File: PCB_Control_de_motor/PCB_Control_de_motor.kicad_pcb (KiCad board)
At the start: 2 copper layers, 71 x 45.5 mm, 50 parts, among them IC1 ESP32-S3-WROOM-1-N16, IC2 USBLC6-2SC6, IC3 DRV8871DDAR, IC4 AP63203WU-7

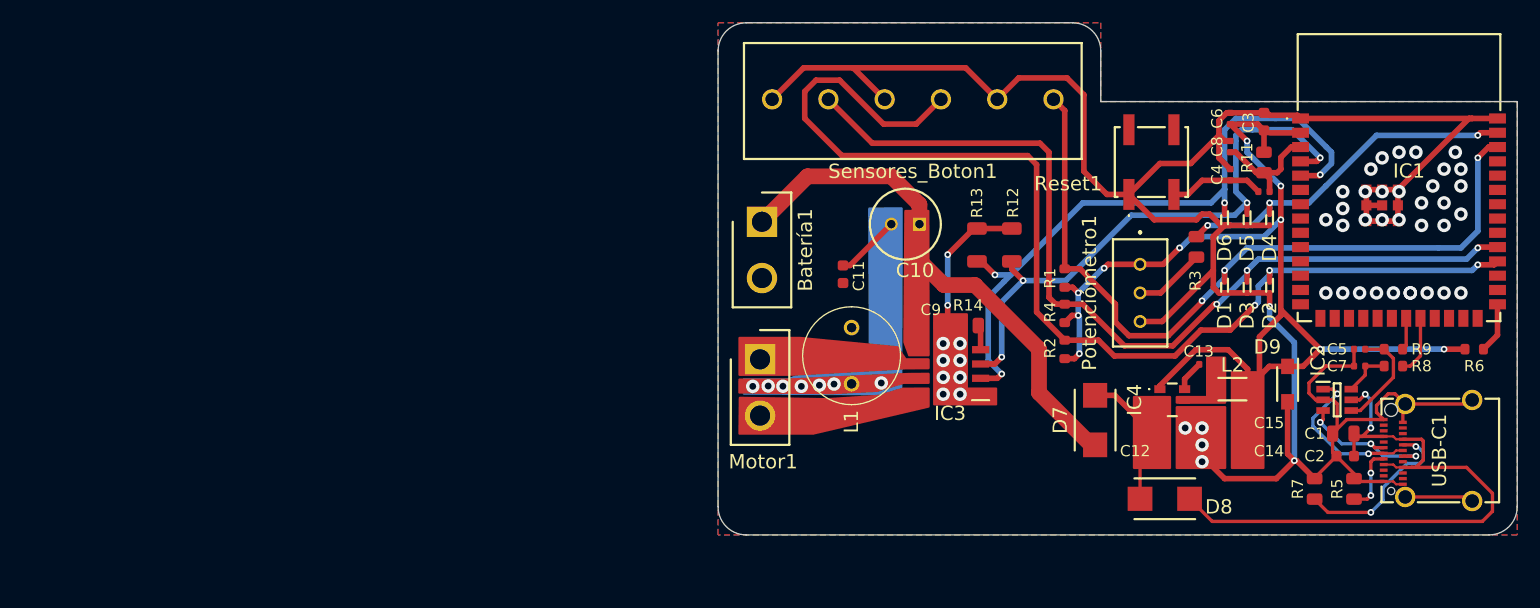
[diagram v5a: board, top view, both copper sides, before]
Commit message: Eliminación de las vías en la bobina del power ground
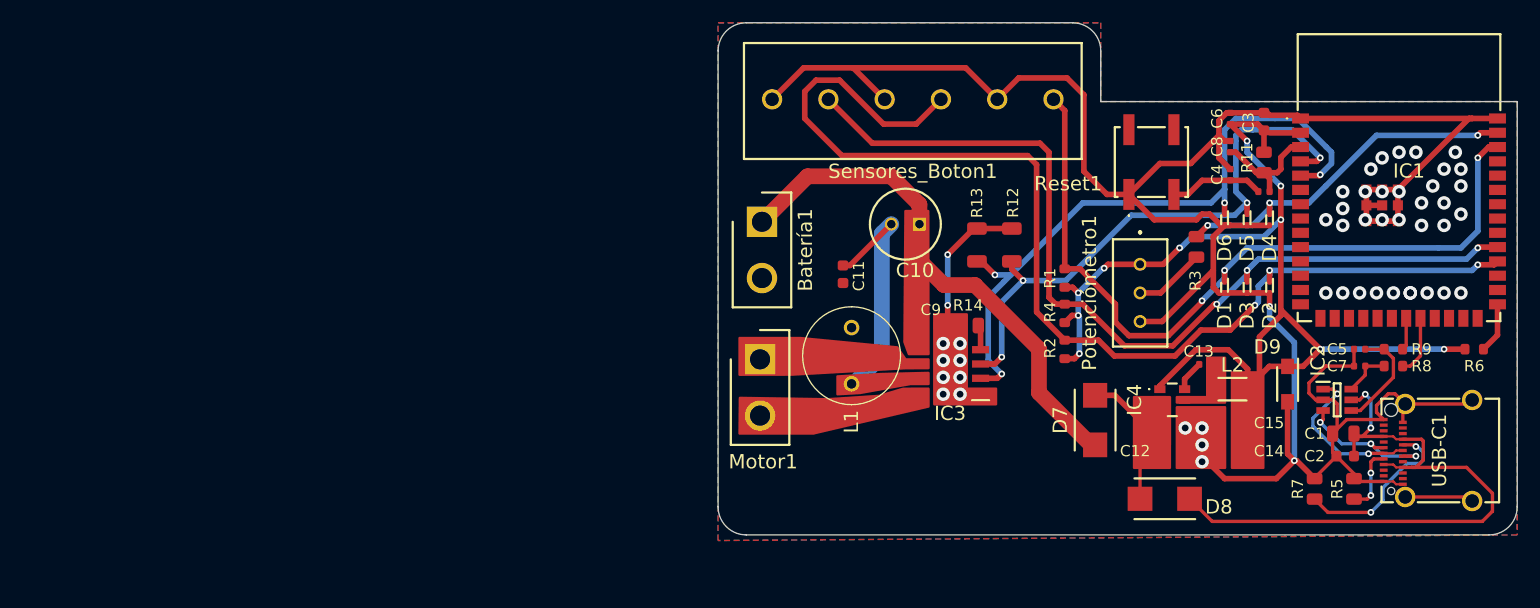
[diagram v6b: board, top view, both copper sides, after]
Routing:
- net Net-(C10--): vias 7 -> 0
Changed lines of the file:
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@@
 	(gr_poly
 		(pts
-			(xy 143.7 103.9) (xy 143.7 102.5) (xy 141.1 102.5) (xy 141.1 95.9) (xy 138.2 95.9) (xy 138.2 103.9)
+			(xy 137.7 101.1) (xy 133.5 101.2) (xy 129.6 101.412727) (xy 129.6 103.011111) (xy 131.6 102.9) (xy 136.1 102.1)
+			(xy 137.7 102.1)
 		)
 		(stroke
@@
 		(fill yes)
 		(layer "F.Cu")
-		(net 1)
+		(net 8)
 	)
 	(gr_poly
 		(pts
-			(xy 137.7 101.189281) (xy 135.92 101.2) (xy 125.158007 101.7) (xy 120.9 101.7) (xy 120.89 102.85)
-			(xy 129.2 102.9) (xy 133.1 102.7) (xy 135.466667 101.99) (xy 137.7 101.99)
+			(xy 143.7 103.9) (xy 143.7 102.5) (xy 141.1 102.5) (xy 141.1 95.9) (xy 138.2 95.9) (xy 138.2 103.9)
 		)
 		(stroke
@@
 		(fill yes)
 		(layer "F.Cu")
-		(net 8)
+		(net 1)
 	)
 	(gr_poly
@@
 	(gr_poly
 		(pts
-			(xy 137.7 99.54) (xy 135.98 99.54) (xy 135.55 98.37) (xy 135.64 86.72) (xy 137.68 86.72)
+			(xy 137.699844 99.44) (xy 135.943248 99.44) (xy 135.55 98.37) (xy 135.64 86.72) (xy 137.68 86.72)
 		)
 		(stroke
@@
 		(net 65)
 	)
-	(gr_poly
-		(pts
-			(xy 121.28 102.94) (xy 135.27 103.01) (xy 135.31 86.49) (xy 132.43 86.51) (xy 132.48 98.59) (xy 125.26 101.68)
-			(xy 121.29 101.69)
-		)
-		(stroke
-			(width 0.2)
-			(type solid)
-		)
-		(fill yes)
-		(layer "B.Cu")
-		(net 8)
-	)
 	(gr_line
 		(start 153 72.5)
@@
 		(layer "Edge.Cuts")
 	)
-	(gr_line
-		(start 119 117.5)
-		(end 119 117.5)
-		(stroke
-			(width 0.05)
-			(type default)
-		)
-		(layer "Edge.Cuts")
-	)
 	(gr_arc
 		(start 190 113)
@@
 		(net 8)
 	)
-	(via
-		(at 126.4 102.3)
-		(size 1.2)
-		(drill 0.6)
-		(layers "F.Cu" "B.Cu")
-		(free yes)
-		(net 8)
-	)
-	(via
-		(at 123.45 102.27)
-		(size 1.2)
-		(drill 0.6)
-		(layers "F.Cu" "B.Cu")
-		(free yes)
-		(net 8)
-	)
-	(via
-		(at 128 102.2)
-		(size 1.2)
-		(drill 0.6)
-		(layers "F.Cu" "B.Cu")
-		(free yes)
-		(net 8)
-	)
-	(via
-		(at 133.5 102)
-		(size 1.2)
-		(drill 0.6)
-		(layers "F.Cu" "B.Cu")
-		(free yes)
-		(net 8)
-	)
-	(via
-		(at 129.3 102.1)
-		(size 1.2)
-		(drill 0.6)
-		(layers "F.Cu" "B.Cu")
-		(free yes)
-		(net 8)
-	)
-	(via
-		(at 122.08 102.3)
-		(size 1.2)
-		(drill 0.6)
-		(layers "F.Cu" "B.Cu")
-		(free yes)
-		(net 8)
-	)
-	(via
-		(at 124.76 102.29)
-		(size 1.2)
-		(drill 0.6)
-		(layers "F.Cu" "B.Cu")
-		(free yes)
-		(net 8)
-	)
 	(segment
 		(start 134.39 87.89)
@@
 		(polygon
 			(pts
-				(xy 119 70) (xy 153 70) (xy 153 77) (xy 190 77) (xy 190 115.5) (xy 119 115.5)
+				(xy 119 70) (xy 153 70) (xy 153 77) (xy 190 77) (xy 190 115.5) (xy 119 116)
 			)
 		)
